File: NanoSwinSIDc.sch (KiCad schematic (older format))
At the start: 14 parts, among them J1 JTAG, U1 C64-SID-Socket, U2 ATMEGA88PA-AU, X1 32Mhz

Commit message: Oscillator should have had a hand-soldering footprint.
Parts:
- X1: footprint Oscillators:Oscillator_SMD_EuroQuartz_XO53-4pin_5.0x3.2mm -> Oscillators:Oscillator_SMD_EuroQuartz_XO53-4pin_5.0x3.2mm_HandSoldering
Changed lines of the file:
@@
 F 0 "X1" H 4650 2750 50  0000 L CNN
 F 1 "32Mhz" H 4600 2650 50  0000 L CNN
-F 2 "Oscillators:Oscillator_SMD_EuroQuartz_XO53-4pin_5.0x3.2mm" H 5150 2550 50  0001 C CNN
+F 2 "Oscillators:Oscillator_SMD_EuroQuartz_XO53-4pin_5.0x3.2mm_HandSoldering" H 5150 2550 50  0001 C CNN
 F 3 "http://cdn-reichelt.de/documents/datenblatt/B400/XO53.pdf" H 4350 2900 50  0001 C CNN
 	1    4450 2900

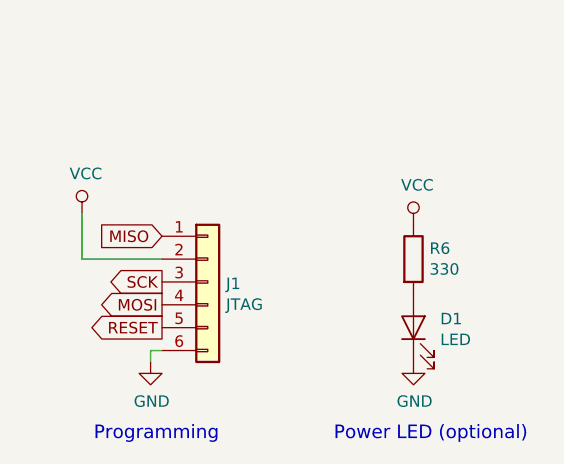
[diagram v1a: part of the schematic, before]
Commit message: Replaced 50mil header with regular 100mil ones and adapted board layout.
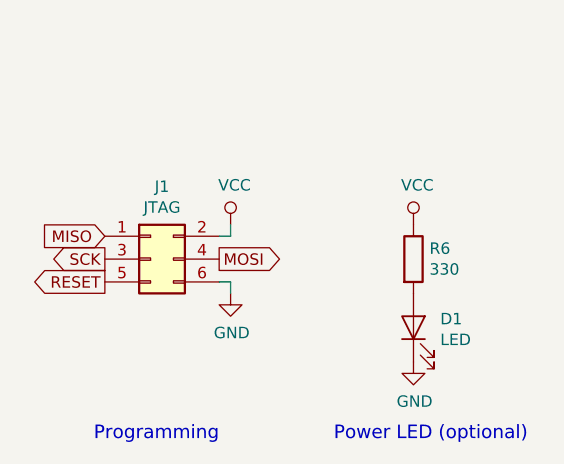
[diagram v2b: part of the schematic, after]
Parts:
- removed J1: JTAG, Pin_Headers:Pin_Header_Straight_1x06_Pitch1.27mm, symbol Connector:Conn_01x06
- added J1: JTAG, Pin_Headers:Pin_Header_Straight_2x03_Pitch2.54mm, symbol Connector:Conn_02x03_Odd_Even
- JP1, JP2: footprint Pin_Headers:Pin_Header_Straight_1x02_Pitch1.27mm -> Pin_Headers:Pin_Header_Angled_1x02_Pitch2.54mm
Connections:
- net GND: now also J1.6 (Pin_6)
- net MISO: now also J1.1 (Pin_1)
- net MOSI: now also J1.4 (Pin_4)
- net RESET: now also J1.5 (Pin_5)
- net SCK: now also J1.3 (Pin_3)
- net VCC: now also J1.2 (Pin_2)
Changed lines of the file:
@@
 Sheet 1 1
 Title "Nano SwinSID c"
-Date "2018-04-06"
-Rev "1"
+Date "2018-04-13"
+Rev "2"
 Comp "hackup.net"
 Comment1 ""
@@
 	1    0    0    -1
 $EndComp
-$Comp
-L Connector:Conn_01x06 J1
-U 1 1 5AC8968B
-P 2100 6200
-F 0 "J1" H 2180 6192 50  0000 L CNN
-F 1 "JTAG" H 2180 6101 50  0000 L CNN
-F 2 "Pin_Headers:Pin_Header_Straight_1x06_Pitch1.27mm" H 2100 6200 50  0001 C CNN
-F 3 "~" H 2100 6200 50  0001 C CNN
-	1    2100 6200
-	1    0    0    -1
-$EndComp
-Text GLabel 1900 6000 0    50   Input ~ 0
+Text GLabel 1650 6000 0    50   Input ~ 0
 MISO
-Text GLabel 1900 6200 0    50   Output ~ 0
+Text GLabel 1650 6100 0    50   Output ~ 0
 SCK
-Text GLabel 1900 6300 0    50   Output ~ 0
+Text GLabel 2150 6100 2    50   Output ~ 0
 MOSI
-Text GLabel 1900 6400 0    50   Output ~ 0
+Text GLabel 1650 6200 0    50   Output ~ 0
 RESET
 $Comp
 L power:GND #PWR0106
 U 1 1 5AC90C4D
-P 1850 6550
-F 0 "#PWR0106" H 1850 6300 50  0001 C CNN
-F 1 "GND" H 1855 6377 50  0000 C CNN
-F 2 "" H 1850 6550 50  0001 C CNN
-F 3 "" H 1850 6550 50  0001 C CNN
-	1    1850 6550
+P 2200 6250
+F 0 "#PWR0106" H 2200 6000 50  0001 C CNN
+F 1 "GND" H 2205 6077 50  0000 C CNN
+F 2 "" H 2200 6250 50  0001 C CNN
+F 3 "" H 2200 6250 50  0001 C CNN
+	1    2200 6250
 	1    0    0    -1
 $EndComp
@@
 L power:VCC #PWR0107
 U 1 1 5AC90C7E
-P 1550 5900
-F 0 "#PWR0107" H 1550 5750 50  0001 C CNN
-F 1 "VCC" H 1567 6073 50  0000 C CNN
-F 2 "" H 1550 5900 50  0001 C CNN
-F 3 "" H 1550 5900 50  0001 C CNN
-	1    1550 5900
-	1    0    0    -1
-$EndComp
-Wire Wire Line
-	1550 5900 1550 6100
-Wire Wire Line
-	1550 6100 1900 6100
-Wire Wire Line
-	1900 6500 1850 6500
-Wire Wire Line
-	1850 6500 1850 6550
+P 2200 5950
+F 0 "#PWR0107" H 2200 5800 50  0001 C CNN
+F 1 "VCC" H 2217 6123 50  0000 C CNN
+F 2 "" H 2200 5950 50  0001 C CNN
+F 3 "" H 2200 5950 50  0001 C CNN
+	1    2200 5950
+	1    0    0    -1
+$EndComp
 Text GLabel 3800 3400 2    39   Input ~ 0
 RESET
@@
 F 0 "JP1" H 4200 2214 50  0000 C CNN
 F 1 "6581SEL" H 4200 2123 50  0000 C CNN
-F 2 "Pin_Headers:Pin_Header_Straight_1x02_Pitch1.27mm" H 4200 1950 50  0001 C CNN
+F 2 "Pin_Headers:Pin_Header_Angled_1x02_Pitch2.54mm" H 4200 1950 50  0001 C CNN
 F 3 "" H 4200 1950 50  0001 C CNN
 	1    4200 1950
@@
 F 0 "JP2" V 7704 2727 50  0000 L CNN
 F 1 "Jumper" V 7795 2727 50  0000 L CNN
-F 2 "Pin_Headers:Pin_Header_Straight_1x02_Pitch1.27mm" H 7750 2600 50  0001 C CNN
+F 2 "Pin_Headers:Pin_Header_Angled_1x02_Pitch2.54mm" H 7750 2600 50  0001 C CNN
 F 3 "" H 7750 2600 50  0001 C CNN
 	1    7750 2600
@@
 Wire Wire Line
 	1850 1950 1850 1850
+$Comp
+L Connector:Conn_02x03_Odd_Even J1
+U 1 1 5AD0F4E2
+P 1850 6100
+F 0 "J1" H 1900 6417 50  0000 C CNN
+F 1 "JTAG" H 1900 6326 50  0000 C CNN
+F 2 "Pin_Headers:Pin_Header_Straight_2x03_Pitch2.54mm" H 1850 6100 50  0001 C CNN
+F 3 "~" H 1850 6100 50  0001 C CNN
+	1    1850 6100
+	1    0    0    -1
+$EndComp
+Wire Wire Line
+	2150 6000 2200 6000
+Wire Wire Line
+	2200 6000 2200 5950
+Wire Wire Line
+	2150 6200 2200 6200
+Wire Wire Line
+	2200 6200 2200 6250
 $EndSCHEMATC

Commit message: Library update.
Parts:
- J1: symbol Connector:Conn_02x03_Odd_Even -> Connector_Generic:Conn_02x03_Odd_Even
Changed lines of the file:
@@
 EESchema Schematic File Version 4
 LIBS:NanoSwinSIDc-cache
-EELAYER 26 0
+EELAYER 29 0
 EELAYER END
 $Descr A4 11693 8268
@@
 	1850 1950 1850 1850
 $Comp
-L Connector:Conn_02x03_Odd_Even J1
+L Connector_Generic:Conn_02x03_Odd_Even J1
 U 1 1 5AD0F4E2
 P 1850 6100
